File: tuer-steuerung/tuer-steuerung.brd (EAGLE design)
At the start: 65.7 x 66 mm, 46 parts, among them IC1 L6203, IC2 MEGA8-P, Q1 20MHz, T1 BC337, T2 BC337, X1 ENDSTOP1, X2 ENDSTOP2, X3 DOORSTATE, X4 LOCKSTATE, X5 MOTOR, X6 NERDSTERN

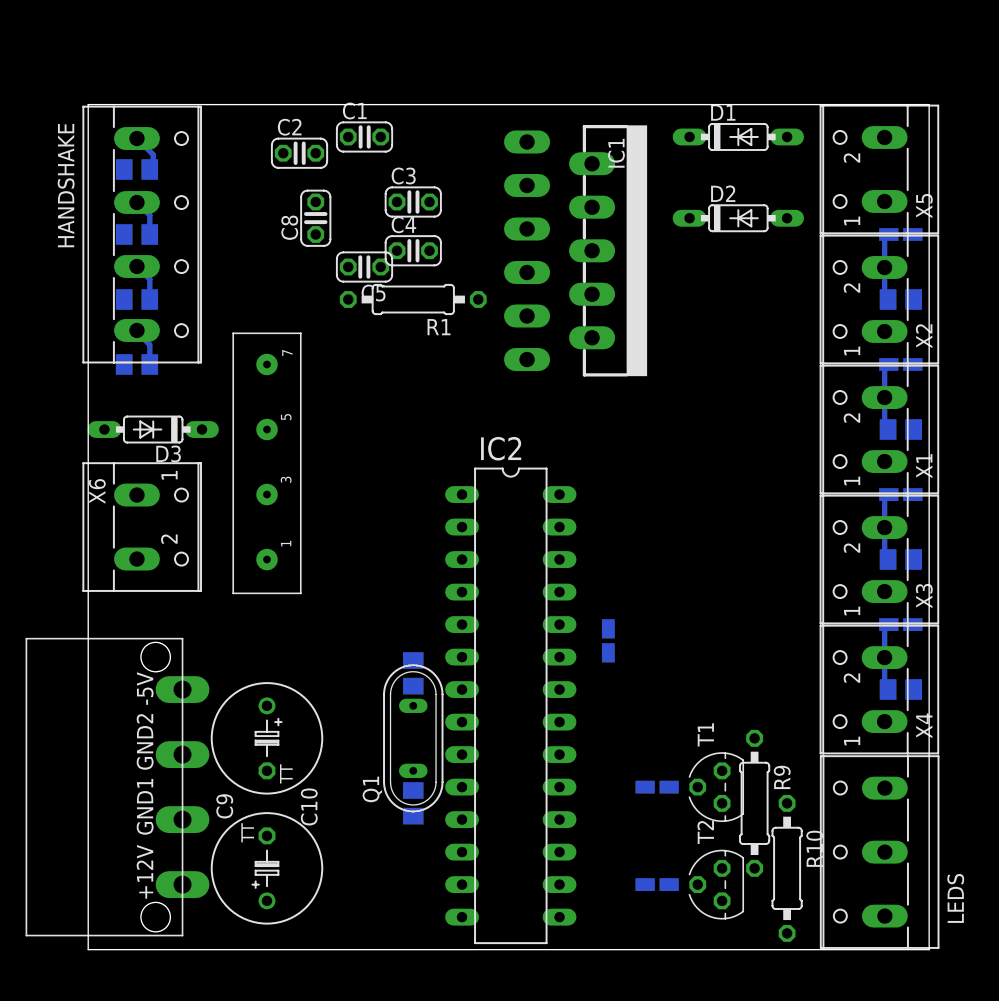
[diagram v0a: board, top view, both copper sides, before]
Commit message: * Kleine Anpassungen in der Schaltung * Layout der Peripherie
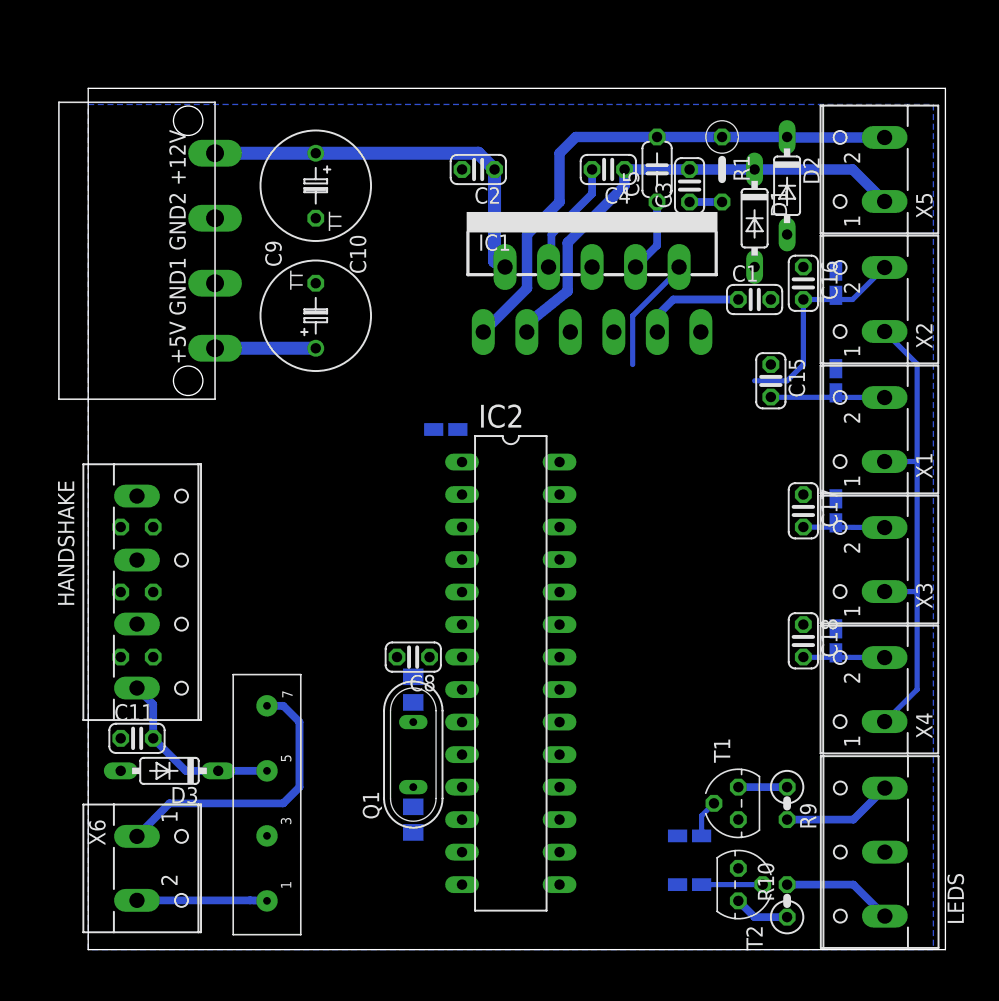
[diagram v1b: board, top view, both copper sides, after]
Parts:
- C11, C12, C13, C14, C15, C16, C17, C18: device resistor:C0805K -> resistor:C025-024X044
- C5: device resistor:C025-024X044 -> resistor:C050-024X044
- Q1: value 20MHz -> 16Mhz
- R1: device resistor:0207/10 -> resistor:0207/5V
- R10, R9: device resistor:0207/10 -> resistor:0207/2V
- moved C9 43.3 mm to (17.8, 49.5)
- moved C10 43.3 mm to (17.8, 59.7)
- moved U$1 42.0 mm to (3.81, 54.6)
- moved C8 35.1 mm to (25.4, 22.9), turned to 180 degrees
- moved C1 33.0 mm to (52.1, 50.8)
- moved C11 29.2 mm to (3.81, 16.5), flipped to the top, turned to 0 degrees
- moved C13 27.9 mm to (3.81, 27.9)
- moved HANDSHAKE 27.9 mm to (5.08, 27.9)
- moved C12 27.9 mm to (3.81, 22.9)
- moved C14 27.9 mm to (3.81, 33.0)
- moved D3 26.7 mm to (6.35, 14.0)
- moved U$2 26.7 mm to (14.0, 11.4)
- moved X6 26.7 mm to (5.08, 6.35)
- moved R1 26.2 mm to (49.5, 61.0), turned to 270 degrees
- moved C5 24.1 mm to (44.5, 61.0), turned to 90 degrees
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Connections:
- net GND: now also C15.1, C16.1, C17.1, C18.1, C8.2, U$2.P3; no longer C8.1, U$2.P5
- net LOCKSTATE: now also C11.2, HANDSHAKE.4, U$2.P5; no longer C14.2, HANDSHAKE.1, U$2.P3
- net M_OUT1: now also X5.1; no longer X5.2
- net M_OUT2: now also X5.2; no longer X5.1
- net SET_OPEN: now also C14.2, HANDSHAKE.1; no longer C11.2, HANDSHAKE.4
- net VCC: now also C8.1, IC2.7, R2.2, U$1.+5V; no longer C15.1, C16.1, C17.1, C18.1, U$1.-5V
- net VDD: no longer C8.2, IC2.7, R2.2
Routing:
- net VCC: track 0.00 -> 45.6 mm
- net M_OUT2: track 0.00 -> 42.4 mm
- net M_OUT1: track 0.00 -> 37.4 mm
- net VDD: track 0.00 -> 30.5 mm
- net N$4: track 0.00 -> 22.5 mm
- net LOCKSTATE: track 8.90 -> 21.1 mm
- net ENDSTOP2: track 5.41 -> 17.1 mm
- net N$5: track 0.00 -> 10.2 mm
- net M_SENSE: track 0.00 -> 9.12 mm
- net N$7: track 0.00 -> 8.96 mm
- net N$14: track 0.00 -> 8.66 mm
- net N$12: track 0.00 -> 8.66 mm
- net N$3: track 0.00 -> 8.19 mm
- net N$8: track 0.00 -> 5.78 mm
- net N$10: track 0.00 -> 4.77 mm
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- added copper zone on layer 16, net GND
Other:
- board size 65.7 x 66 mm -> 67 x 67.3 mm

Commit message: Alex' Verbesserungen eingearbeitet und Layout fortgesetzt
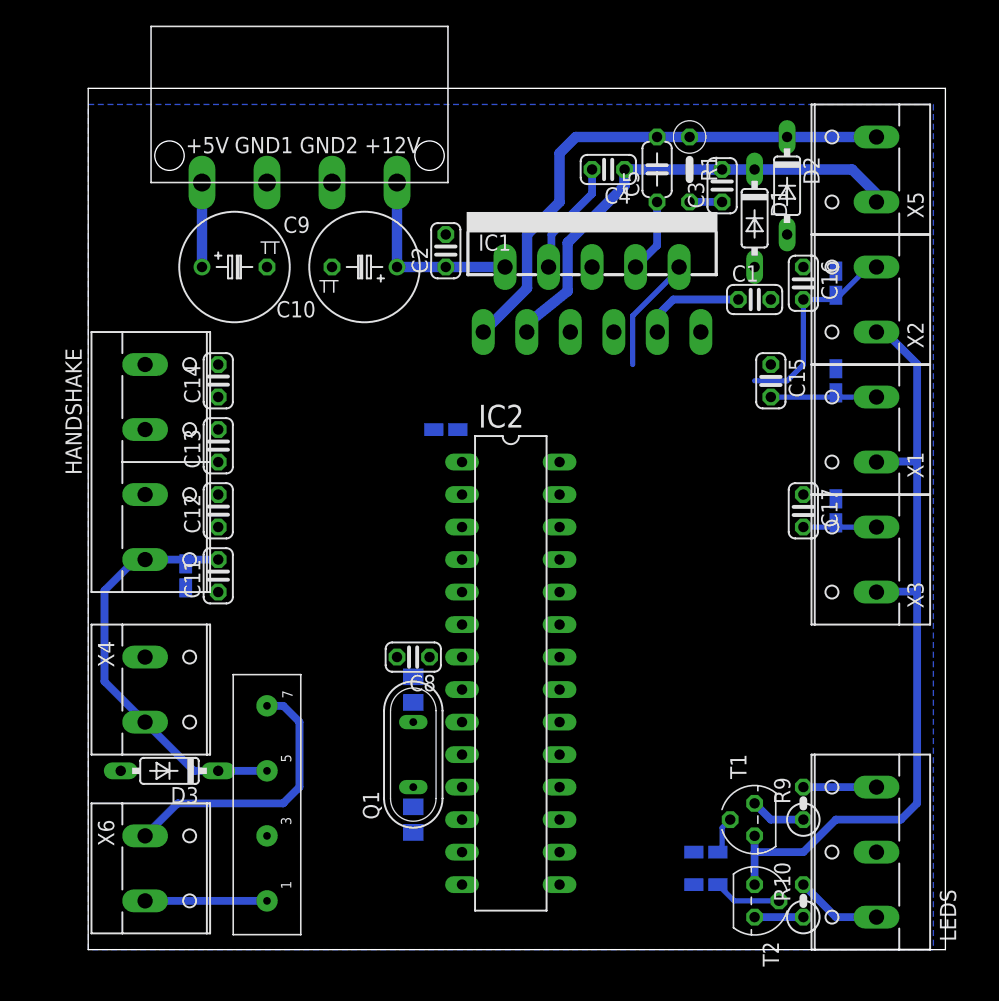
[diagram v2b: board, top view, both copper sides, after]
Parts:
- removed C18: 100n, resistor:C025-024X044
- C3: value 100n -> 22n
- C4, C5: value 100n -> 15n
- HANDSHAKE: device con-wago-500:W237-4 -> con-wago-508:W237-4P
- LEDS: device con-wago-500:W237-103 -> con-wago-508:W237-133
- R1: value (none) -> 10R
- X1, X2, X3, X4, X5, X6: device con-wago-500:W237-102 -> con-wago-508:W237-132
- moved X4 55.9 mm to (5.08, 20.3), turned to 270 degrees
- moved R6 51.1 mm to (7.62, 29.2), turned to 270 degrees
- moved U$1 17.1 mm to (16.5, 66.0), turned to 0 degrees
- moved C11 14.2 mm to (10.2, 29.2), turned to 90 degrees
- moved C12 13.1 mm to (10.2, 34.3), flipped to the top, turned to 90 degrees
- moved C14 13.1 mm to (10.2, 44.5), flipped to the top, turned to 90 degrees
- moved C13 13.1 mm to (10.2, 39.4), flipped to the top, turned to 90 degrees
- moved HANDSHAKE 10.2 mm to (5.08, 38.1)
- moved C9 7.41 mm to (11.4, 53.3), turned to 0 degrees
- moved C10 7.41 mm to (21.6, 53.3), turned to 180 degrees
- moved C2 6.84 mm to (27.9, 54.6), turned to 90 degrees
- moved C3 2.54 mm to (49.5, 59.7)
- moved R1 2.54 mm to (47.0, 61.0)
- moved T2 1.80 mm to (52.1, 3.81)
- moved T1 1.80 mm to (52.1, 10.2)
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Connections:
- net DOORSTATE: now also IC2.11; no longer IC2.3
- net GND: no longer C18.1, T1.3, T2.3
- net LOCKSTATE: now also IC2.6; no longer C18.2, IC2.2
- net M_SENSE: no longer IC2.23
- net VCC: now also T1.3, T2.3
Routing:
- net VCC: track 45.6 -> 69.6 mm
- net VDD: track 30.5 -> 15.0 mm
- net LOCKSTATE: track 21.1 -> 32.9 mm
- net N$12: track 8.66 -> 5.71 mm
- net N$14: track 8.66 -> 6.77 mm
- net M_OUT2: track 42.4 -> 41.7 mm
- net ENDSTOP1: track 9.25 -> 8.58 mm
- net N$4: track 22.5 -> 21.8 mm
- net N$5: track 10.2 -> 9.53 mm
- net DOORSTATE: track 6.70 -> 6.06 mm
- net ENDSTOP2: track 17.1 -> 16.5 mm
- net N$10: track 4.77 -> 5.30 mm
- net N$13: track 4.34 -> 3.81 mm
- net N$11: track 3.81 -> 4.34 mm

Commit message: Layout vollständig (nur 3 Drahtbrücken! \o/)
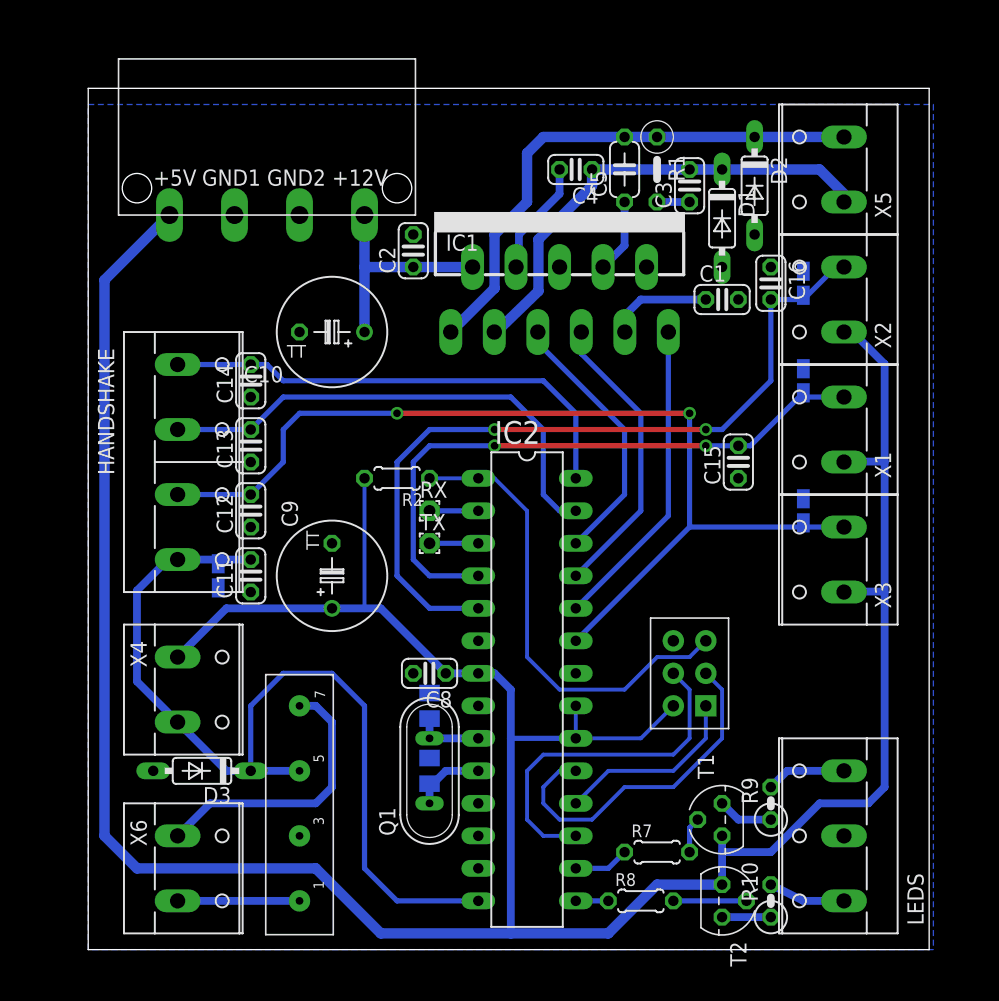
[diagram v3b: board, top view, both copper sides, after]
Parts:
- removed C17: 100n, resistor:C025-024X044
- added RX, TX: (no value), wirepad:1,6/0,9
- added U$3: AVR_ISP, n39:AVR_ISP
- R2, R7, R8: device resistor:R0805W -> resistor:0204/5
- moved C9 25.3 mm to (19.1, 29.2), turned to 90 degrees
- moved C15 6.84 mm to (50.8, 38.1), turned to 90 degrees
- moved C10 5.68 mm to (19.1, 48.3)
- moved R2 5.39 mm to (24.1, 36.8), flipped to the top, turned to 180 degrees
- moved R8 5.24 mm to (43.2, 3.81), flipped to the top, turned to 0 degrees
- moved C6 4.02 mm to (26.7, 14.0), turned to 90 degrees
- moved R7 3.81 mm to (44.5, 7.62), flipped to the top, turned to 0 degrees
- moved U$1 3.59 mm to (14.0, 63.5)
- moved LEDS 2.84 mm to (58.4, 8.89)
- moved C5 2.54 mm to (41.9, 61.0)
- moved C2 2.54 mm to (25.4, 54.6)
- moved D3 2.54 mm to (8.89, 14.0)
- moved U$2 2.54 mm to (16.5, 11.4)
- moved HANDSHAKE 2.54 mm to (7.62, 38.1)
- moved R6 2.54 mm to (10.2, 29.2)
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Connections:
- removed net AVCC: IC2.20
- new net N$15: IC2.3, TX.1
- new net N$16: IC2.2, RX.1
- net DOORSTATE: now also C12.2, HANDSHAKE.3, IC2.23; no longer C13.2, C17.2, HANDSHAKE.2, IC2.11
- net GND: now also U$3.GND; no longer C17.1
- net LED_G: now also IC2.16; no longer IC2.28
- net LED_R: now also IC2.15; no longer IC2.27
- net LOCKSTATE: now also IC2.14; no longer IC2.6
- net MISO: now also U$3.MISO
- net MOSI: now also U$3.MOSI
- net RST: now also U$3.RST
- net SCK: now also U$3.SCK
- net SET_CLOSE: now also C13.2, HANDSHAKE.2, IC2.27; no longer C12.2, HANDSHAKE.3, IC2.14
- net SET_OPEN: now also IC2.28; no longer IC2.15
- net VCC: now also IC2.20, IC2.21, U$3.VCC
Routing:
- net VCC: track 69.6 -> 243.5 mm
- net DOORSTATE: track 6.06 -> 78.1 mm, vias 0 -> 2
- net ENDSTOP2: track 16.5 -> 61.6 mm, vias 0 -> 2
- net ENDSTOP1: track 8.58 -> 49.5 mm, vias 0 -> 2
- net SET_CLOSE: track 0.00 -> 38.8 mm
- net LOCKSTATE: track 32.9 -> 71.6 mm
- net SET_OPEN: track 0.00 -> 37.8 mm
- net RST: track 0.00 -> 36.7 mm
- net MOSI: track 0.00 -> 27.5 mm
- net SCK: track 0.00 -> 27.1 mm
- net M_EN: track 0.00 -> 24.6 mm
- net M_IN1: track 0.00 -> 23.1 mm
- net M_IN2: track 0.00 -> 20.9 mm
- net MISO: track 0.00 -> 14.8 mm
- net M_SENSE: track 9.12 -> 0.00 mm
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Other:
- board size 67 x 67.3 mm -> 65.7 x 67.3 mm

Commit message: Anschlussklemmen angepasst
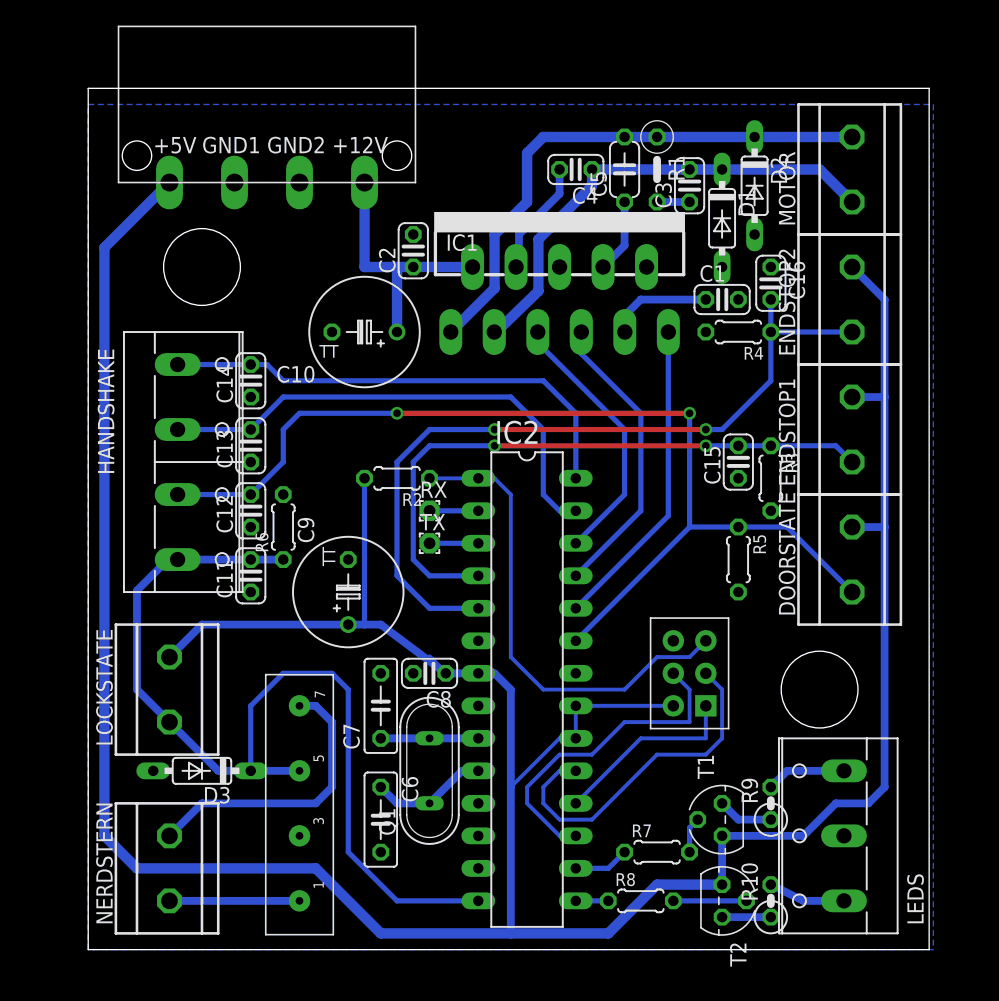
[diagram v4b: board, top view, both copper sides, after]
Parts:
- removed X1: ENDSTOP1, con-wago-508:W237-132
- removed X2: ENDSTOP2, con-wago-508:W237-132
- removed X3: DOORSTATE, con-wago-508:W237-132
- removed X4: LOCKSTATE, con-wago-508:W237-132
- removed X5: MOTOR, con-wago-508:W237-132
- removed X6: NERDSTERN, con-wago-508:W237-132
- added DOORSTATE, ENDSTOP1, ENDSTOP2, LOCKSTATE, MOTOR, NERDSTERN: RIACON_101_2, n39:RIACON_101_2
- C6, C7: device resistor:C0805K -> resistor:C050-025X075
- R3, R4, R5, R6: device resistor:R0805W -> resistor:0204/5
- moved R3 8.03 mm to (53.3, 36.8), flipped to the top, turned to 270 degrees
- moved R4 6.35 mm to (50.8, 48.3), flipped to the top, turned to 180 degrees
- moved R5 6.35 mm to (50.8, 30.5), flipped to the top, turned to 270 degrees
- moved R6 6.35 mm to (15.2, 33.0), flipped to the top, turned to 90 degrees
- moved C6 5.39 mm to (22.9, 10.2), flipped to the top, turned to 270 degrees
- moved C7 3.81 mm to (22.9, 19.1), flipped to the top
- moved U$1 2.54 mm to (14.0, 66.0)
- moved C10 2.54 mm to (21.6, 48.3)
- moved C9 1.80 mm to (20.3, 27.9)
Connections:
- net DOORSTATE: now also DOORSTATE.1; no longer X3.2
- net ENDSTOP1: now also ENDSTOP1.1; no longer X1.2
- net ENDSTOP2: now also ENDSTOP2.1; no longer X2.2
- net LOCKSTATE: now also LOCKSTATE.1; no longer X4.2
- net M_OUT1: now also MOTOR.1; no longer X5.1
- net M_OUT2: now also MOTOR.2; no longer X5.2
- net N$4: now also NERDSTERN.2; no longer X6.1
- net N$5: now also NERDSTERN.1; no longer X6.2
- net VCC: now also DOORSTATE.2, ENDSTOP1.2, ENDSTOP2.2, LOCKSTATE.2; no longer X1.1, X2.1, X3.1, X4.1
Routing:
- net VCC: track 243.5 -> 249.6 mm
- net N$1: track 5.76 -> 9.20 mm
- net LOCKSTATE: track 71.6 -> 74.2 mm
- net VDD: track 17.6 -> 20.1 mm
- net N$2: track 5.35 -> 7.62 mm
- net DOORSTATE: track 78.1 -> 80.4 mm
- net MOSI: track 27.5 -> 25.3 mm
- net ENDSTOP1: track 49.5 -> 48.6 mm
- net ENDSTOP2: track 61.6 -> 60.8 mm
- net RST: track 36.7 -> 37.4 mm
- net N$5: track 9.53 -> 10.2 mm
- net N$4: track 21.8 -> 22.4 mm
- net M_OUT2: track 41.7 -> 42.4 mm
